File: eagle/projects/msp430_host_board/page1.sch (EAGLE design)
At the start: 28 parts, among them U1 Value, U2 PCT2075D,118, U3 MS560702BA03-50, Y1 32.768kHz, Y2 4MHz

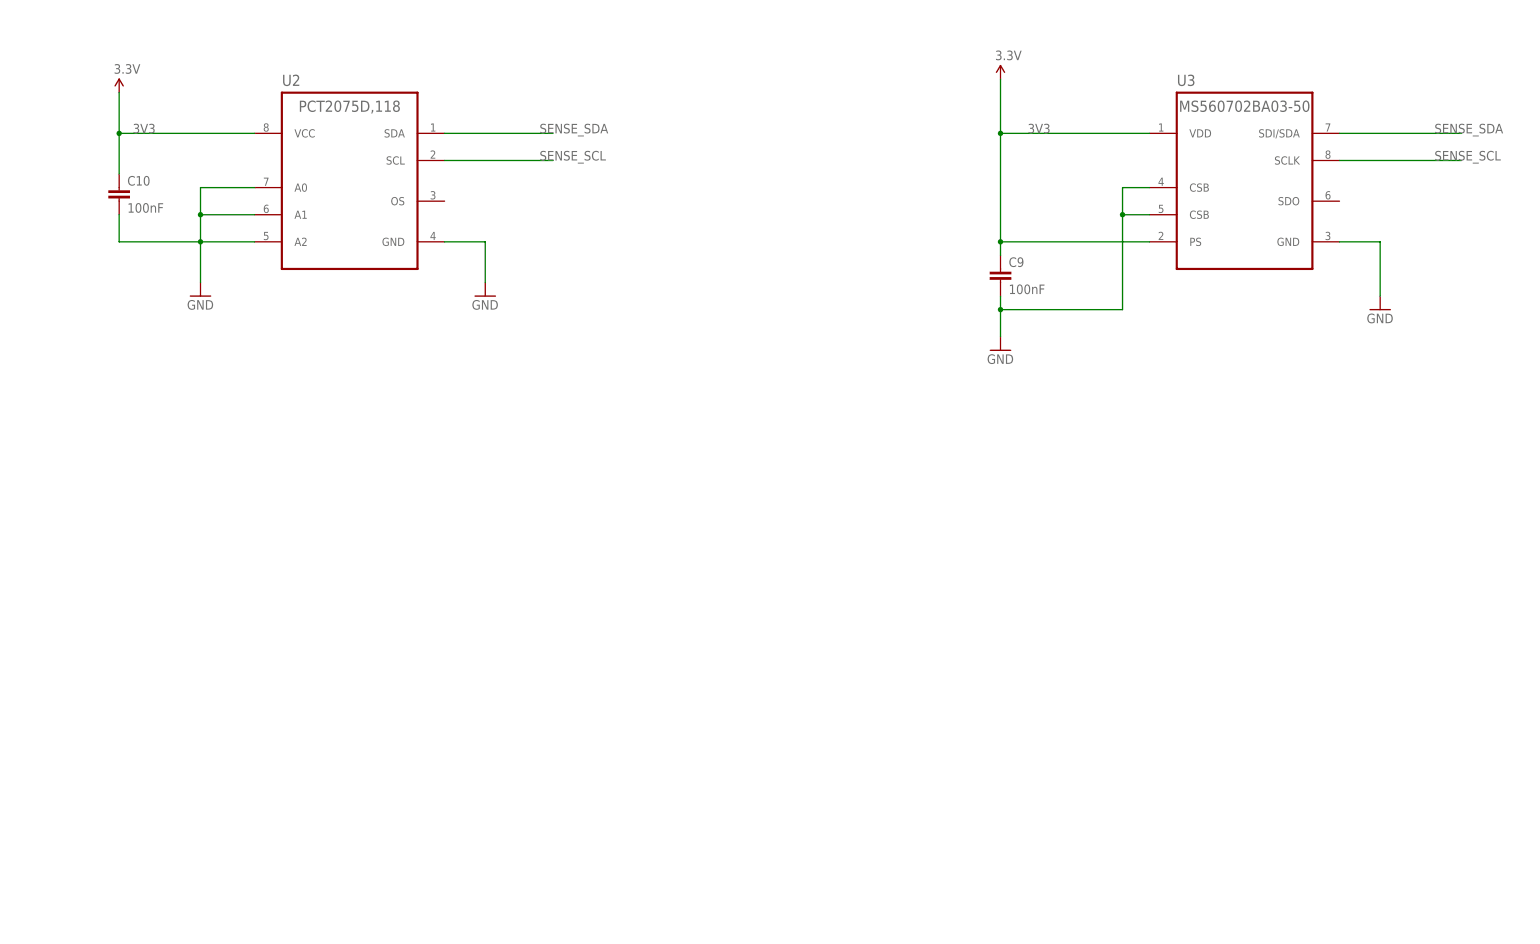
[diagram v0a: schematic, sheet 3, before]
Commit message: Added Samtec connector library to Element14 folder. Added IMU connector
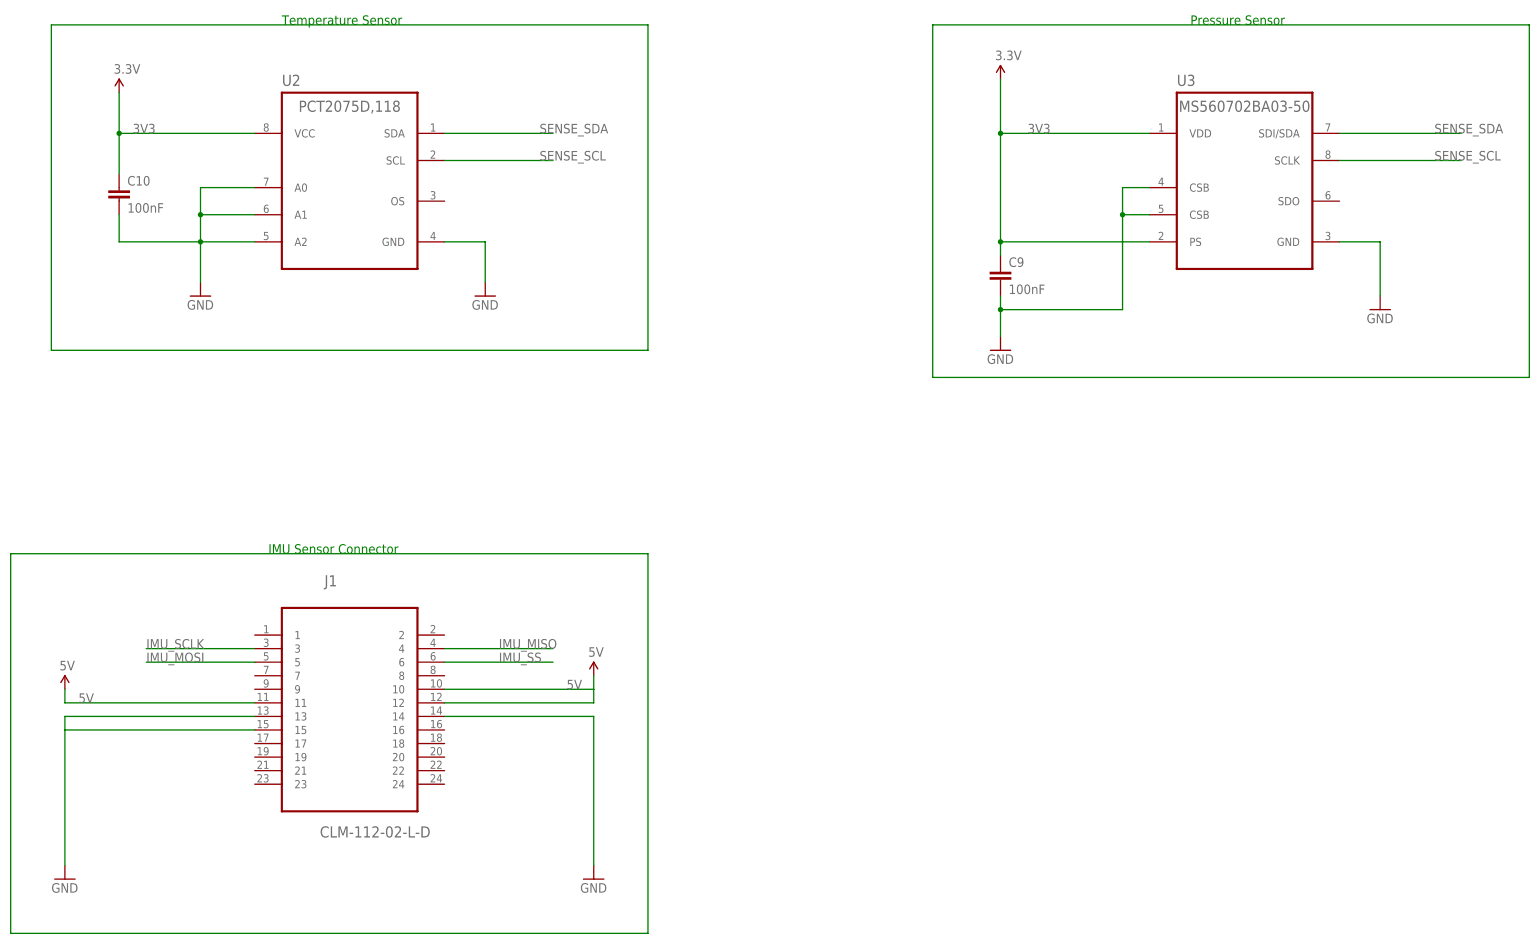
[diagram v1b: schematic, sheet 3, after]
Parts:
- added J1: CLM-112-02-L-D, SAMTEC-BCS-CES-CLx_By_element14_Batch_1:CLM-112-02-L-D
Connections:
- new net 5V: J1.10, J1.11, J1.12
- net GND: now also J1.13, J1.14, J1.15
- net IMU_MISO: now also J1.4
- net IMU_MOSI: now also J1.5
- net IMU_SCLK: now also J1.3
- net IMU_SS: now also J1.6
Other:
- note added: "IMU Sensor Connector"
- note added: "Pressure Sensor"
- note added: "Temperature Sensor"
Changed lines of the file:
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@@
 <part name="R4" library="daqcs_host" deviceset="RES" device="_0603" technology="_2R61" value="2.61k"/>
 <part name="SUPPLY5" library="SparkFun-Aesthetics" deviceset="3.3V" device=""/>
+<part name="J1" library="SAMTEC-BCS-CES-CLx_By_element14_Batch_1" deviceset="CLM-112-02-L-D" device=""/>
+<part name="SUPPLY6" library="SparkFun-Aesthetics" deviceset="5V" device=""/>
+<part name="SUPPLY7" library="SparkFun-Aesthetics" deviceset="5V" device=""/>
+<part name="GND10" library="SparkFun-Aesthetics" deviceset="GND" device=""/>
+<part name="GND11" library="SparkFun-Aesthetics" deviceset="GND" device=""/>
 </parts>
 <sheets>
@@
 <instances>
 <instance part="U1" gate="A" x="43.18" y="48.26">
-<attribute name="MANUFACTURER" x="43.18" y="48.26" size="1.778" layer="96"/>
-<attribute name="PARTNUMBER" x="43.18" y="48.26" size="1.778" layer="96" display="off"/>
+<attribute name="MANUFACTURER" x="43.18" y="48.26" size="1.778" layer="96" display="off"/>
+<attribute name="PARTNUMBER" x="43.18" y="48.26" size="1.778" layer="96"/>
 </instance>
 <instance part="3V3" gate="G$1" x="-71.12" y="114.3"/>
@@
 <sheet>
 <plain>
+<text x="45.72" y="190.5" size="1.778" layer="91">Temperature Sensor</text>
+<text x="215.9" y="190.5" size="1.778" layer="91">Pressure Sensor</text>
+<text x="43.18" y="91.44" size="1.778" layer="91">IMU Sensor Connector</text>
 </plain>
 <instances>
@@
 <instance part="C9" gate="G$1" x="180.34" y="142.24"/>
 <instance part="C10" gate="G$1" x="15.24" y="157.48"/>
+<instance part="J1" gate="A" x="58.42" y="66.04"/>
+<instance part="SUPPLY6" gate="G$1" x="5.08" y="66.04"/>
+<instance part="SUPPLY7" gate="G$1" x="104.14" y="68.58"/>
+<instance part="GND10" gate="1" x="5.08" y="30.48"/>
+<instance part="GND11" gate="1" x="104.14" y="30.48"/>
 </instances>
 <busses>
@@
 <junction x="180.34" y="137.16"/>
 </segment>
+<segment>
+<pinref part="J1" gate="A" pin="13"/>
+<wire x1="40.64" y1="60.96" x2="5.08" y2="60.96" width="0.1524" layer="91"/>
+<pinref part="GND10" gate="1" pin="GND"/>
+<wire x1="5.08" y1="60.96" x2="5.08" y2="58.42" width="0.1524" layer="91"/>
+<pinref part="J1" gate="A" pin="15"/>
+<wire x1="5.08" y1="58.42" x2="5.08" y2="33.02" width="0.1524" layer="91"/>
+<wire x1="40.64" y1="58.42" x2="5.08" y2="58.42" width="0.1524" layer="91"/>
+</segment>
+<segment>
+<pinref part="J1" gate="A" pin="14"/>
+<wire x1="76.2" y1="60.96" x2="104.14" y2="60.96" width="0.1524" layer="91"/>
+<pinref part="GND11" gate="1" pin="GND"/>
+<wire x1="104.14" y1="60.96" x2="104.14" y2="33.02" width="0.1524" layer="91"/>
+</segment>
 </net>
 <net name="SENSE_SDA" class="0">
@@
 </segment>
 </net>
+<net name="IMU_SCLK" class="0">
+<segment>
+<pinref part="J1" gate="A" pin="3"/>
+<wire x1="40.64" y1="73.66" x2="20.32" y2="73.66" width="0.1524" layer="91"/>
+<label x="20.32" y="73.66" size="1.778" layer="95"/>
+</segment>
+</net>
+<net name="5V" class="0">
+<segment>
+<pinref part="SUPPLY6" gate="G$1" pin="5V"/>
+<wire x1="5.08" y1="66.04" x2="5.08" y2="63.5" width="0.1524" layer="91"/>
+<pinref part="J1" gate="A" pin="11"/>
+<wire x1="40.64" y1="63.5" x2="5.08" y2="63.5" width="0.1524" layer="91"/>
+<label x="7.62" y="63.5" size="1.778" layer="95"/>
+</segment>
+<segment>
+<pinref part="J1" gate="A" pin="12"/>
+<wire x1="76.2" y1="63.5" x2="104.14" y2="63.5" width="0.1524" layer="91"/>
+<pinref part="SUPPLY7" gate="G$1" pin="5V"/>
+<wire x1="104.14" y1="63.5" x2="104.14" y2="66.04" width="0.1524" layer="91"/>
+<pinref part="J1" gate="A" pin="10"/>
+<wire x1="104.14" y1="66.04" x2="104.14" y2="68.58" width="0.1524" layer="91"/>
+<wire x1="76.2" y1="66.04" x2="104.14" y2="66.04" width="0.1524" layer="91"/>
+<label x="99.06" y="66.04" size="1.778" layer="95"/>
+</segment>
+</net>
+<net name="IMU_MISO" class="0">
+<segment>
+<pinref part="J1" gate="A" pin="4"/>
+<wire x1="76.2" y1="73.66" x2="96.52" y2="73.66" width="0.1524" layer="91"/>
+<label x="86.36" y="73.66" size="1.778" layer="95"/>
+</segment>
+</net>
+<net name="IMU_MOSI" class="0">
+<segment>
+<pinref part="J1" gate="A" pin="5"/>
+<wire x1="40.64" y1="71.12" x2="20.32" y2="71.12" width="0.1524" layer="91"/>
+<label x="20.32" y="71.12" size="1.778" layer="95"/>
+</segment>
+</net>
+<net name="IMU_SS" class="0">
+<segment>
+<pinref part="J1" gate="A" pin="6"/>
+<wire x1="76.2" y1="71.12" x2="96.52" y2="71.12" width="0.1524" layer="91"/>
+<label x="86.36" y="71.12" size="1.778" layer="95"/>
+</segment>
+</net>
+<net name="N$14" class="0">
+<segment>
+<wire x1="2.54" y1="190.5" x2="114.3" y2="190.5" width="0.1524" layer="91"/>
+<wire x1="114.3" y1="190.5" x2="114.3" y2="129.54" width="0.1524" layer="91"/>
+<wire x1="114.3" y1="129.54" x2="2.54" y2="129.54" width="0.1524" layer="91"/>
+<wire x1="2.54" y1="129.54" x2="2.54" y2="190.5" width="0.1524" layer="91"/>
+</segment>
+</net>
+<net name="N$15" class="0">
+<segment>
+<wire x1="167.64" y1="190.5" x2="279.4" y2="190.5" width="0.1524" layer="91"/>
+<wire x1="279.4" y1="190.5" x2="279.4" y2="124.46" width="0.1524" layer="91"/>
+<wire x1="279.4" y1="124.46" x2="167.64" y2="124.46" width="0.1524" layer="91"/>
+<wire x1="167.64" y1="124.46" x2="167.64" y2="190.5" width="0.1524" layer="91"/>
+</segment>
+</net>
+<net name="N$16" class="0">
+<segment>
+<wire x1="-5.08" y1="91.44" x2="114.3" y2="91.44" width="0.1524" layer="91"/>
+<wire x1="114.3" y1="91.44" x2="114.3" y2="20.32" width="0.1524" layer="91"/>
+<wire x1="114.3" y1="20.32" x2="-5.08" y2="20.32" width="0.1524" layer="91"/>
+<wire x1="-5.08" y1="20.32" x2="-5.08" y2="91.44" width="0.1524" layer="91"/>
+</segment>
+</net>

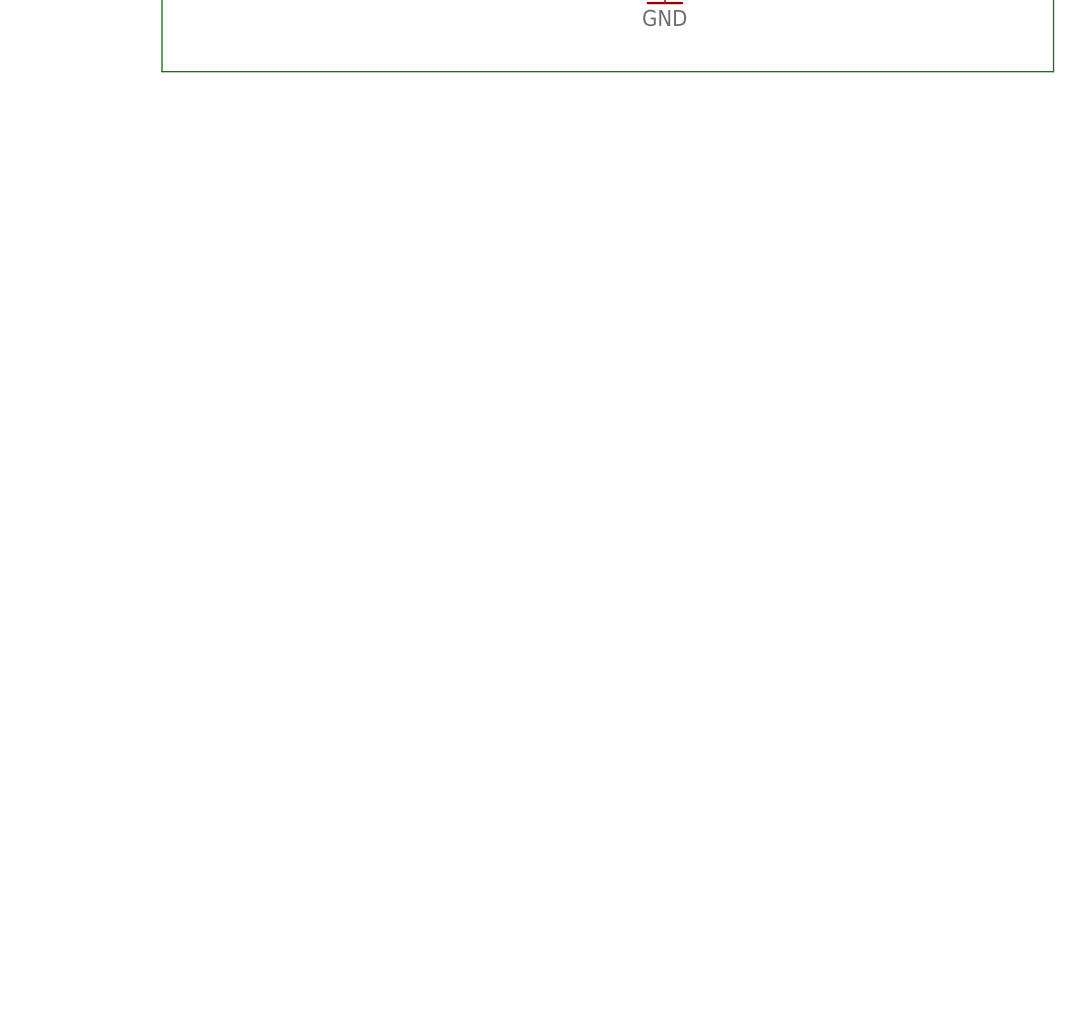
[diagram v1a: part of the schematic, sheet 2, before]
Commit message: Added uSD connector and necessary caps and res for uSD circuit
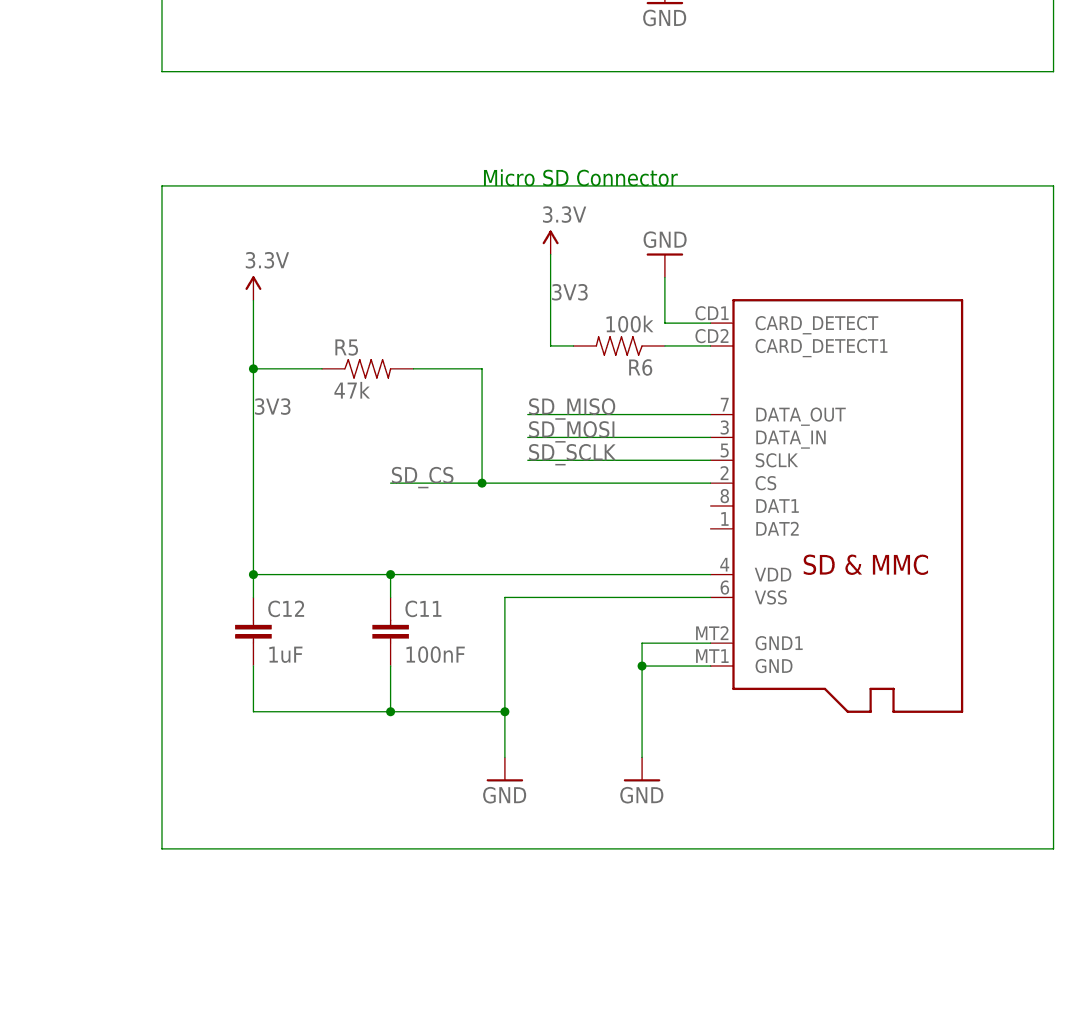
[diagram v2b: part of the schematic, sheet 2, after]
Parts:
- added C11: 100nF, daqcs_host:CAP_100NF0_0603
- added C12: 1uF, daqcs_host:CAP_1UF0_0603
- added J2: (no value), SparkFun-Connectors:M02PTH
- added R5: 47k, daqcs_host:RES_47R0_0603
- added R6: 100k, daqcs_host:RES_100R0_0603
- added U$1: MICROSD, daqcs_host:MICROSD
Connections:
- new net IMU_RST: J2.2, U1.P5.3_UCB1STE
- new net N$17: J1.8, J2.1
- new net N$18: R6.1, U$1.CARD_DETECT1
- net 3V3: now also C11.1, C12.1, R5.1, R6.2, U$1.VDD
- net GND: now also C11.2, C12.2, U$1.CARD_DETECT, U$1.GND, U$1.GND1, U$1.VSS
- net SD_CS: now also R5.2, U$1.CS
- net SD_MISO: now also U$1.DATA_OUT
- net SD_MOSI: now also U$1.DATA_IN
- net SD_SCLK: now also U$1.SCLK
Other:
- note added: "Jumper Header to disable reset ability if necessary"
- note added: "Micro SD Connector"

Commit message: Added 0 res to sensors
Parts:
- added R10, R11, R12, R13, R7, R8, R9: 0, daqcs_host:RES_0R0_0603
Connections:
- new net N$20: R7.1, U2.A0
- new net N$21: R8.2, U2.A1
- new net N$22: R9.2, U2.A2
- new net N$23: R11.2, U3.CSB@1
- new net N$24: R12.2, U3.CSB@2
- new net N$25: R13.1, U3.SDO
- new net N$26: R10.1, U2.OS
- new net N$27: R10.2
- new net N$28: R13.2
- net GND: now also R11.1, R12.1, R7.2, R8.1, R9.1; no longer U2.A0, U2.A1, U2.A2, U3.CSB@1, U3.CSB@2
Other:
- moved on the sheet: C10, C9
